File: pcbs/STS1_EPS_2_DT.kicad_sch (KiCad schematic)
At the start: 19 parts, among them Q2 SI7272DP-T1-GE3, Q3 2N7002, U1 4072, U2 LTC6995IDCB-1

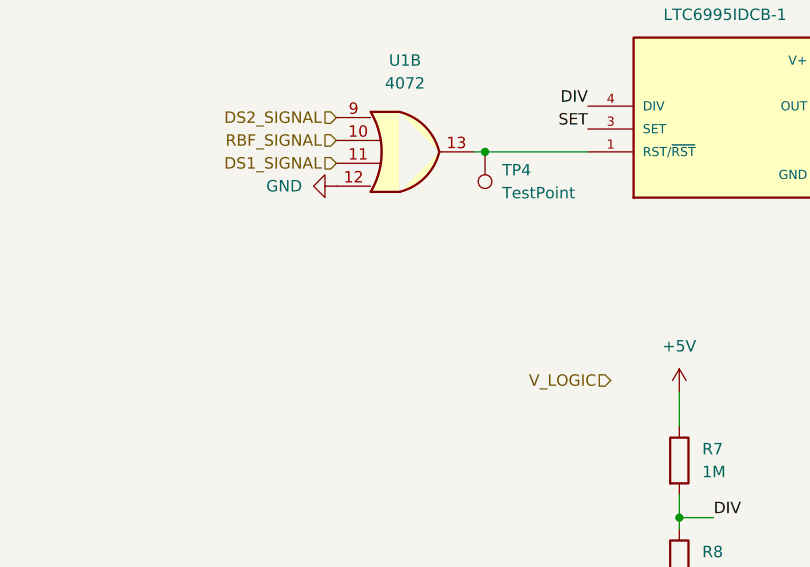
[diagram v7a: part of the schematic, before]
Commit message: Added even more ESD protection.
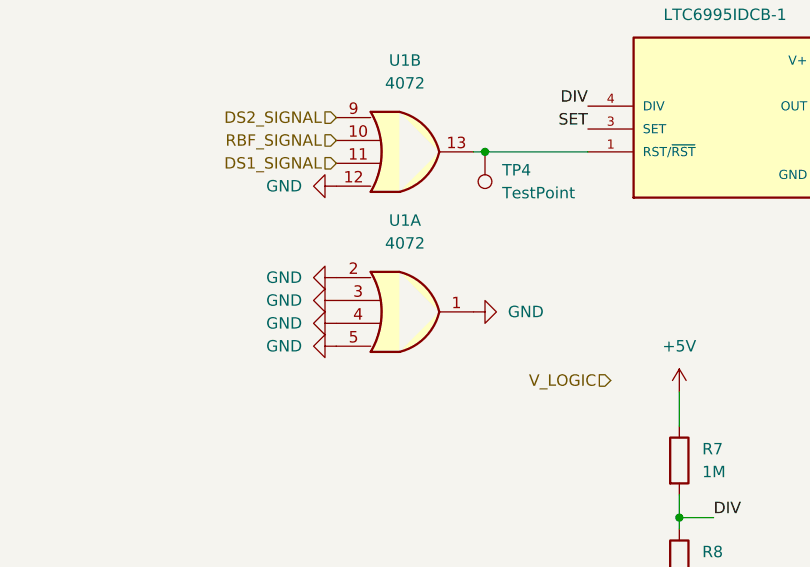
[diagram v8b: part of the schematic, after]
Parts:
- added unit 1 of U1
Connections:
- net GND: now also U1.1, U1.2, U1.3, U1.4, U1.5
